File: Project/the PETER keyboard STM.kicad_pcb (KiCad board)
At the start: 2 copper layers, 243.3 x 95.4 mm, 142 parts, among them J3 USB_C_Receptacle_USB2.0, SW1 RotaryEncoder_Switch, SW12 RotaryEncoder_Switch, SW3 SKQGABE010, U2 STM32F072C8Tx, U3 XC6206PxxxMR-Regulator_Linear, U4 USBLC6-2SC6

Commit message: production files STM
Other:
- board text added: "JLCJLCJLCJLC"

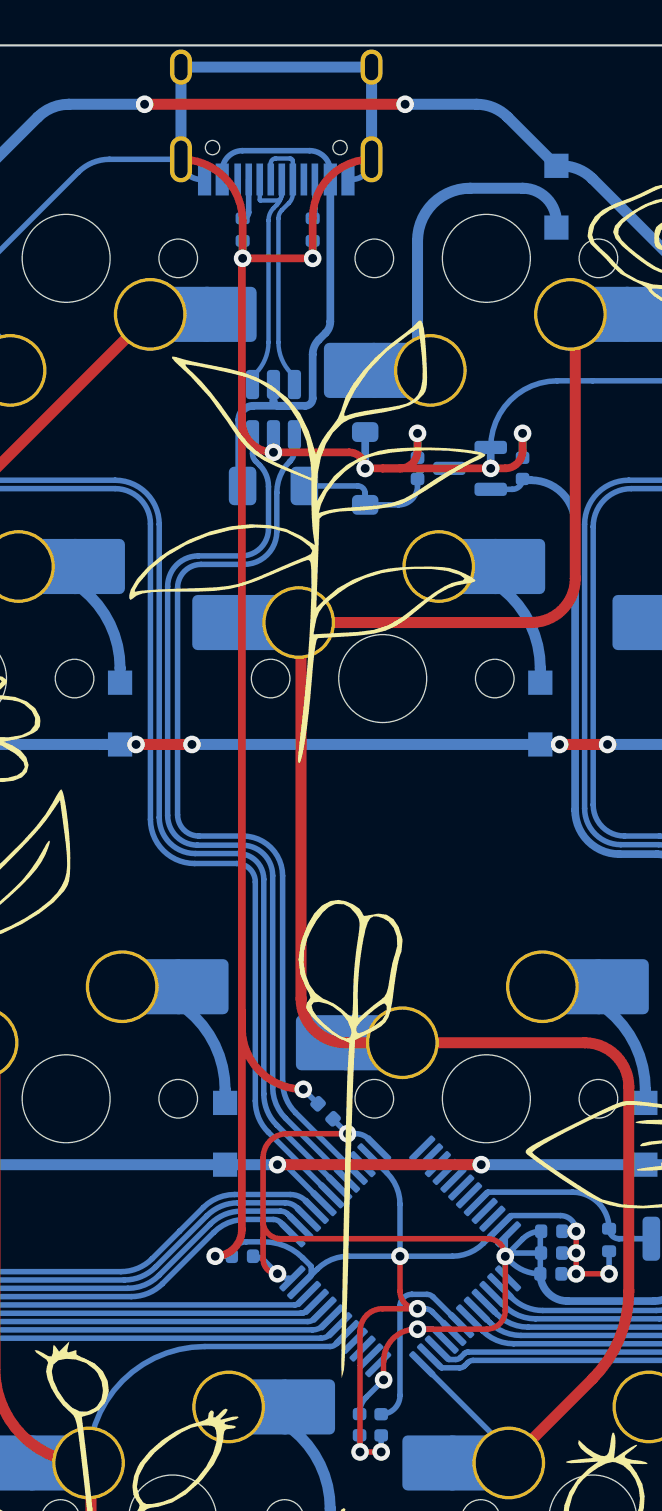
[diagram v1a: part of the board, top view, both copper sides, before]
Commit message: kicad 9
gnd zones
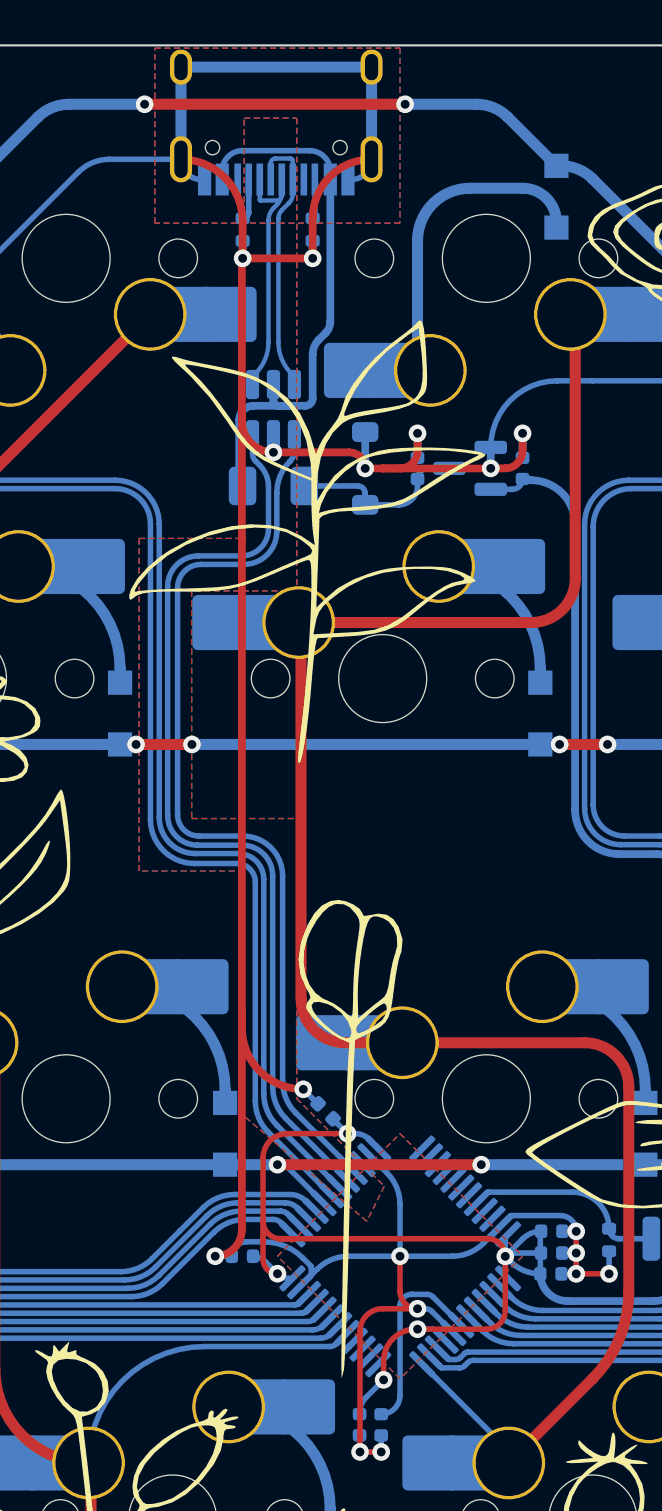
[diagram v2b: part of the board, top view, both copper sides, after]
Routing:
- added copper zone on B.Cu, net (none)
- added copper zone on F.Cu, net (none)
- added copper zone on B.Cu, net GND
- added copper zone on F.Cu, net GND
